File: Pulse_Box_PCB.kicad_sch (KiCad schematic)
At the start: 35 parts, among them J1 Barrel_Jack, J2 Conn_02x05_Odd_Even, J3 USB_B_Micro, J4 Conn_01x03_Pin, U1 STM32F407VGTx, U2 SN74LV1T34DBV, U3 AP2112K-3.3, U4 TPSM53604RDA, Y1 8MHz Crystal

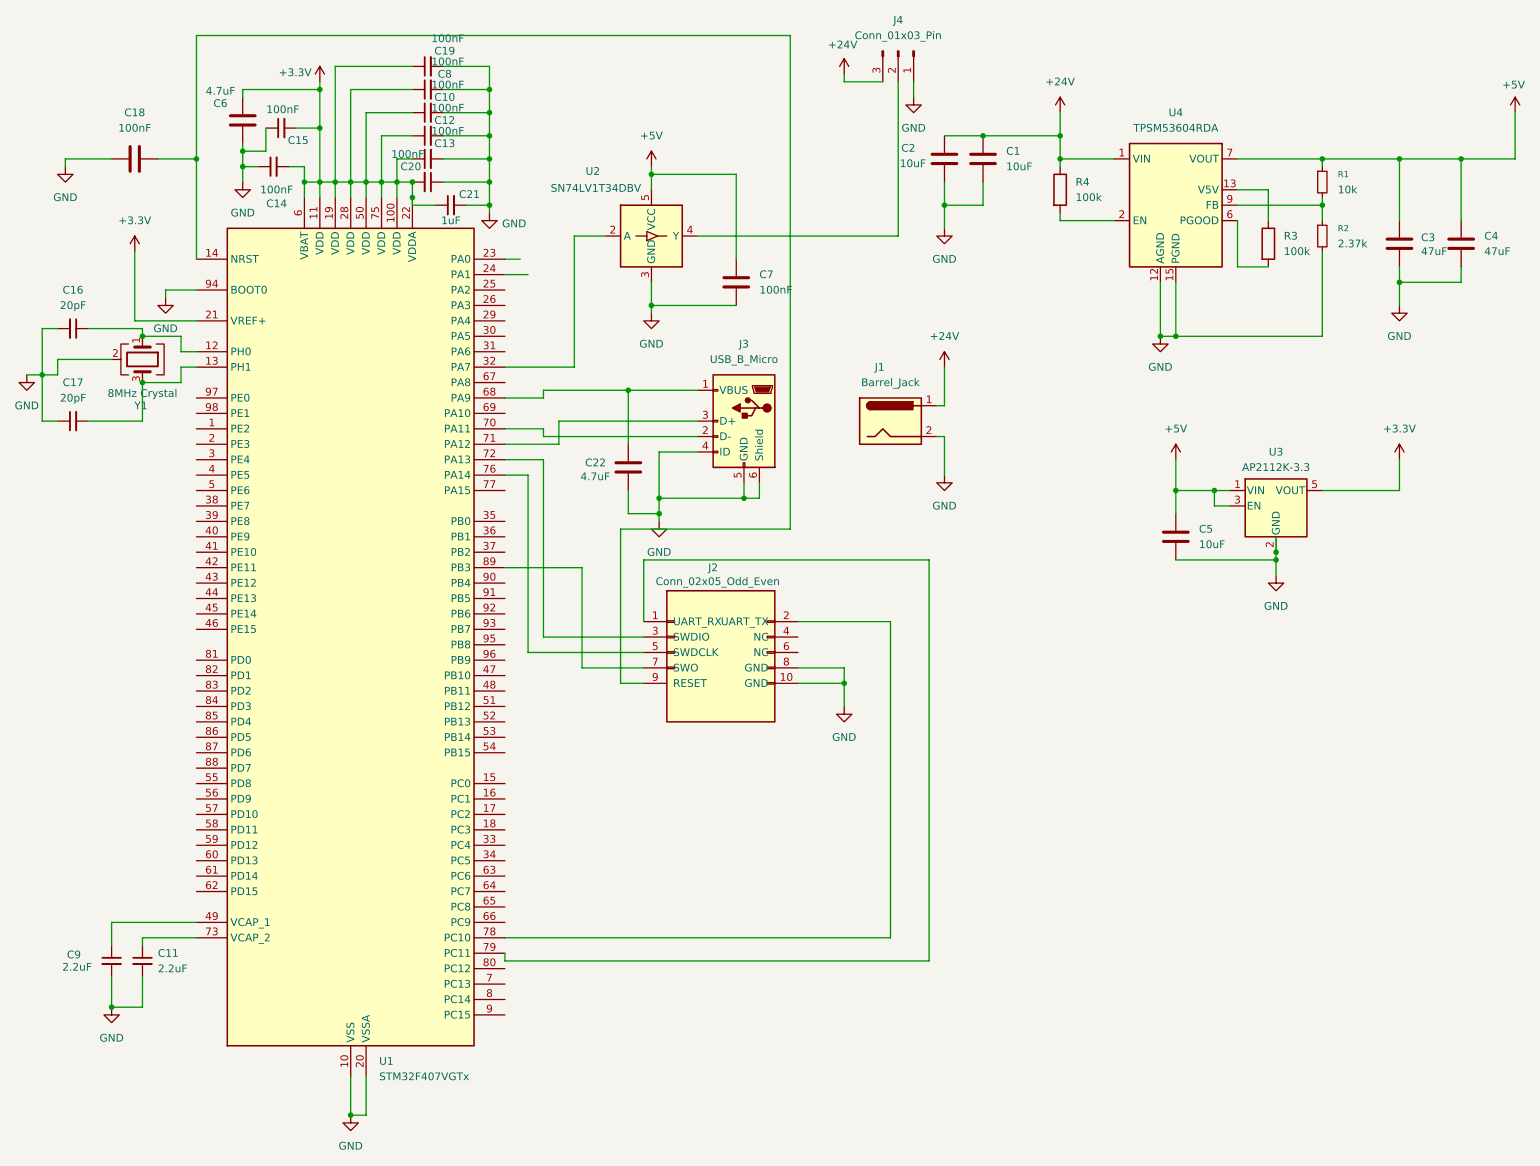
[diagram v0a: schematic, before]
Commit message: organize schematic into power and signal pages, fixed wire nests
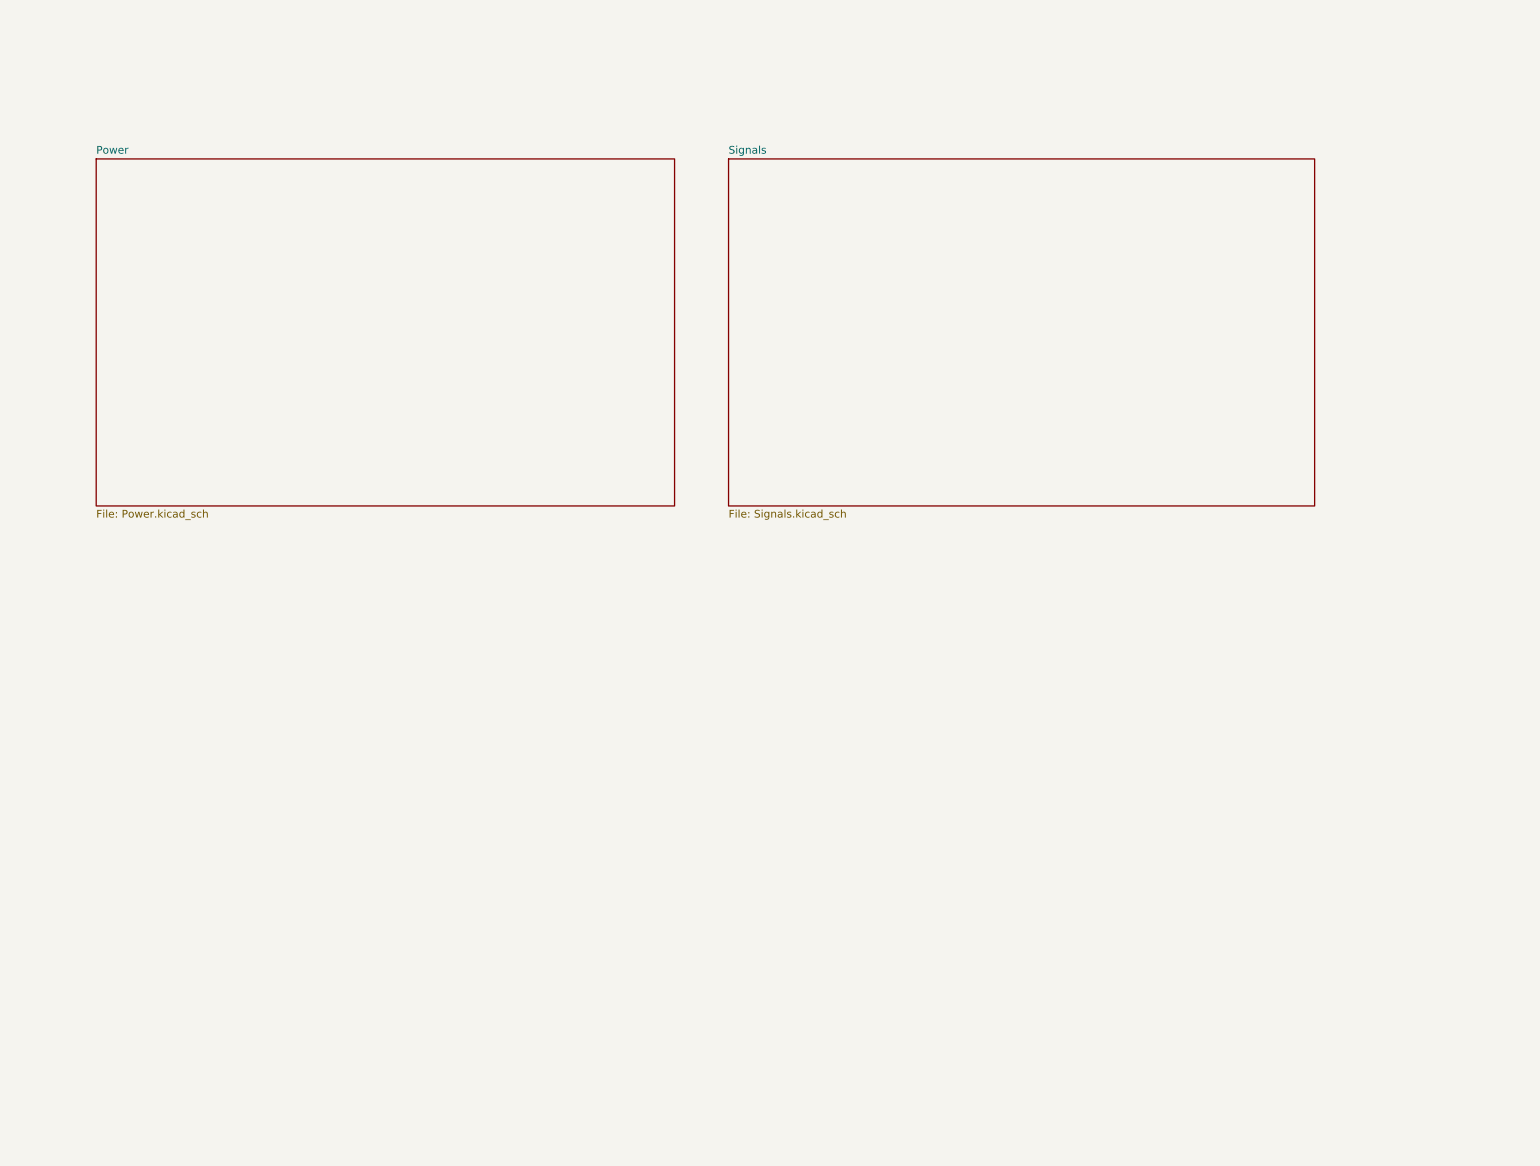
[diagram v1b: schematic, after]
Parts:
- removed C1, C2, C5: 10uF, Capacitor_SMD:C_0805_2012Metric, symbol Device:C
- removed C10, C12, C13, C14, C15, C19, C20, C8: 100nF, Capacitor_SMD:C_0402_1005Metric, symbol Device:C_Small
- removed C11, C9: 2.2uF, Capacitor_SMD:C_0603_1608Metric, symbol Device:C_Small
- removed C16, C17: 20pF, Capacitor_SMD:C_0402_1005Metric, symbol Device:C_Small
- removed C18, C7: 100nF, Capacitor_SMD:C_0402_1005Metric, symbol Device:C
- removed C21: 1uF, Capacitor_SMD:C_0402_1005Metric, symbol Device:C_Small
- removed C22, C6: 4.7uF, Capacitor_SMD:C_0805_2012Metric, symbol Device:C
- removed C3, C4: 47uF, Capacitor_SMD:C_1210_3225Metric, symbol Device:C
- removed J1: Barrel_Jack, Library:XKB_DC-005-5A-2.0, symbol Connector:Barrel_Jack
- removed J2: Conn_02x05_Odd_Even, Connector_PinHeader_1.27mm:PinHeader_2x05_P1.27mm_Vertical, symbol Connector_Generic:Conn_02x05_Odd_Even
- removed J3: USB_B_Micro, Connector_USB:USB_Micro-B_Amphenol_10103594-0001LF_Horizontal, symbol Connector:USB_B_Micro
- removed J4: Conn_01x03_Pin, Connector_PinHeader_2.54mm:PinHeader_1x03_P2.54mm_Vertical, symbol Connector:Conn_01x03_Pin
- removed R1: 10k, Resistor_SMD:R_0402_1005Metric, symbol Device:R_Small
- removed R2: 2.37k, Resistor_SMD:R_0402_1005Metric, symbol Device:R_Small
- removed R3, R4: 100k, Resistor_SMD:R_0402_1005Metric, symbol Device:R
- removed U1: STM32F407VGTx, Package_QFP:LQFP-100_14x14mm_P0.5mm, symbol MCU_ST_STM32F4:STM32F407VGTx
- removed U2: SN74LV1T34DBV, Package_TO_SOT_SMD:SOT-23-5, symbol Logic_LevelTranslator:SN74LV1T34DBV
- removed U3: AP2112K-3.3, Package_TO_SOT_SMD:SOT-23-5, symbol Regulator_Linear:AP2112K-3.3
- removed U4: TPSM53604RDA, Package_DFN_QFN:Texas_B3QFN-14-1EP_5x5.5mm_P0.65mm_ThermalVia, symbol Converter_DCDC:TPSM53604RDA
- removed Y1: 8MHz Crystal, Crystal:Crystal_SMD_3225-4Pin_3.2x2.5mm, symbol Device:Crystal_GND24
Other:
- added sheet Power (Power.kicad_sch)
- added sheet Signals (Signals.kicad_sch)
- title: (none) -> PulseBox Controller PCB
